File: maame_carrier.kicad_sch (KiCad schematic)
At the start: 43 parts, among them J1 To Kakute H7 V1.5: left strip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, J10 FS-iA10B iBUS servo lead (S +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, J11 TF-Luna pin order 1-6 (CFG ti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, J12 Spare FC I2C (5 V supply, sha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, J13 Payload servo power (+ -); se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, J17 Kakute spare: T3 RSSI 3V3(FC)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, J18 Pi SPI0, 3V3 logic, J3 VBAT tap from ESC battery pad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, J6 Spare power: 5V_AUX G 5V_FC G, J7 Pi expansion: 3V3 logic ONLY, J8 TBS M10Q: order matches its p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, J9 SiK radio (UART4), U1 Raspberry Pi Zero W v1.1, com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, U2 TPS54360BDDAR 60V 3.5A buck

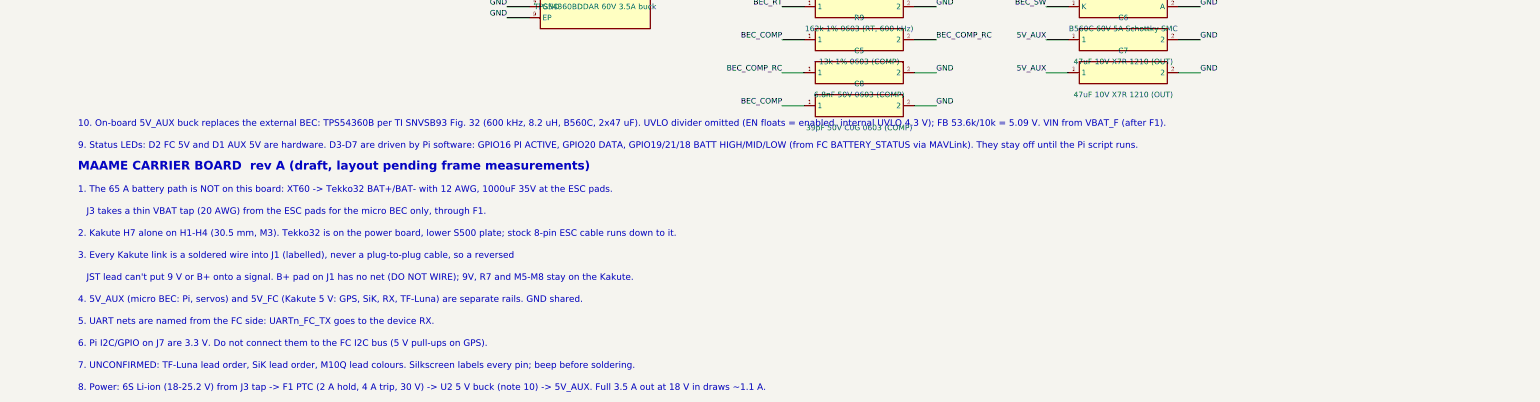
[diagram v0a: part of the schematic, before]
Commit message: D9 SMBJ30A TVS (C113998) on fused VBAT at the buck input; re-routed, DRC 0 errors; fab files regenerated
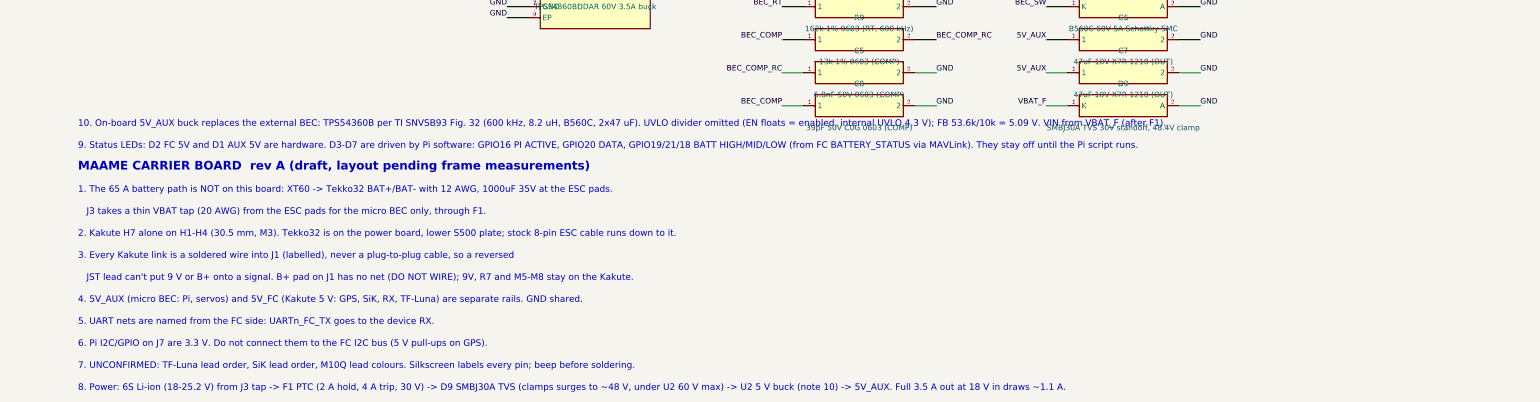
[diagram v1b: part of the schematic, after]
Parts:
- added D9: SMBJ30A TVS 30V standoff, 48.4V clamp, Diode_SMD:D_SMB, symbol maame_carrier:TVS
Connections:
- net GND: now also D9.2 (A)
- net VBAT_F: now also D9.1 (K)
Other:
- note added: "8. Power: 6S Li-ion (18-25.2 V) from J3 tap -> F1 PTC (2 A hold, 4 A trip, 30 V) -> D9 SMBJ30A TVS (clamps surges to ~48 V, under U2 60 V max) -> U2 5 V buck (note 10) -> 5V_AUX. Full 3.5 A out at 18 V in draws ~1.1 A."
- note removed: "8. Power: 6S Li-ion (18-25.2 V) from J3 tap -> F1 PTC (2 A hold, 4 A trip, 30 V) -> U2 5 V buck (note 10) -> 5V_AUX. Full 3.5 A out at 18 V in draws ~1.1 A."
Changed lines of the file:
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@@
 		)
 	)
-	(text "8. Power: 6S Li-ion (18-25.2 V) from J3 tap -> F1 PTC (2 A hold, 4 A trip, 30 V) -> U2 5 V buck (note 10) -> 5V_AUX. Full 3.5 A out at 18 V in draws ~1.1 A."
+	(text "8. Power: 6S Li-ion (18-25.2 V) from J3 tap -> F1 PTC (2 A hold, 4 A trip, 30 V) -> D9 SMBJ30A TVS (clamps surges to ~48 V, under U2 60 V max) -> U2 5 V buck (note 10) -> 5V_AUX. Full 3.5 A out at 18 V in draws ~1.1 A."
 		(exclude_from_sim no)
 		(at 20.32 294.64 0)
@@
 		)
 	)
+	(symbol
+		(lib_id "maame_carrier:TVS")
+		(at 261.62 228.6 0)
+		(unit 1)
+		(body_style 1)
+		(exclude_from_sim no)
+		(in_bom yes)
+		(on_board yes)
+		(in_pos_files yes)
+		(dnp no)
+		(property "Reference" "D9"
+			(at 261.62 223.52 0)
+			(show_name no)
+			(do_not_autoplace no)
+			(effects
+				(font
+					(size 1.27 1.27)
+				)
+			)
+		)
+		(property "Value" "SMBJ30A TVS 30V standoff, 48.4V clamp"
+			(at 261.62 233.68 0)
+			(show_name no)
+			(do_not_autoplace no)
+			(effects
+				(font
+					(size 1.27 1.27)
+				)
+			)
+		)
+		(property "Footprint" "Diode_SMD:D_SMB"
+			(at 261.62 228.6 0)
+			(hide yes)
+			(show_name no)
+			(do_not_autoplace no)
+			(effects
+				(font
+					(size 1.27 1.27)
+				)
+			)
+		)
+		(property "Datasheet" ""
+			(at 261.62 228.6 0)
+			(hide yes)
+			(show_name no)
+			(do_not_autoplace no)
+			(effects
+				(font
+					(size 1.27 1.27)
+				)
+			)
+		)
+		(property "Description" ""
+			(at 261.62 228.6 0)
+			(hide yes)
+			(show_name no)
+			(do_not_autoplace no)
+			(effects
+				(font
+					(size 1.27 1.27)
+				)
+			)
+		)
+		(property "LCSC" "C113998"
+			(at 261.62 228.6 0)
+			(hide yes)
+			(show_name no)
+			(do_not_autoplace no)
+			(effects
+				(font
+					(size 1.27 1.27)
+				)
+			)
+		)
+		(pin "1"
+		)
+		(pin "2"
+		)
+		(instances
+			(project "maame_carrier"
+				(path "/347efe6d-e5df-5320-8613-16be4824f8d1"
+					(reference "D9")
+					(unit 1)
+				)
+			)
+		)
+	)
 	(wire
 		(pts
@@
 			)
 			(justify left bottom)
+		)
+	)
+	(wire
+		(pts
+			(xy 248.92 228.6) (xy 243.84 228.6)
+		)
+		(stroke
+			(width 0)
+			(type default)
+		)
+	)
+	(label "VBAT_F"
+		(at 243.84 228.6 180)
+		(effects
+			(font
+				(size 1.27 1.27)
+			)
+			(justify right bottom)
+		)
+	)
+	(wire
+		(pts
+			(xy 274.32 228.6) (xy 279.4 228.6)
+		)
+		(stroke
+			(width 0)
+			(type default)
+		)
+	)
+	(label "GND"
+		(at 279.4 228.6 0)
+		(effects
+			(font
+				(size 1.27 1.27)
+			)
+			(justify left bottom)

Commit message: Battery labels (6S Li-ion/LiPo 18-25.2 V); J20 VBAT OUT JST-XH via its own F2 2 A PTC; re-routed, DRC 0 errors; fab files regenerated
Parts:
- added F2: PTC fuse 1812 30V 2A hold 4A trip (BSMD1812-200-3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, Fuse:Fuse_1812_4532Metric_Pad1.30x3.40mm_HandSolder, symbol maame_carrier:Fuse
- added J20: VBAT OUT 6S fused (JST-XH 2-pin), Connector_JST:JST_XH_B2B-XH-A_1x02_P2.50mm_Vertical, symbol maame_carrier:BEC_OUT
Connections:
- net GND: now also J20.2 (OUT-)
- net VBAT: now also F2.1
- new net VBAT_OUT_F: F2.2, J20.1 (OUT+)
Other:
- note added: "8. Power: 6S Li-ion (18-25.2 V) from J3 tap -> F1 PTC (2 A hold, 4 A trip, 30 V) -> D9 SMBJ30A TVS (clamps surges to ~48 V, under U2 60 V max) -> U2 5 V buck (note 10) -> 5V_AUX. J20 VBAT OUT (JST-XH) takes VBAT before F1 through its own F2 (2 A). Battery: 6S Li-ion/LiPo only, 18-25.2 V (22.2 V nom). Full 3.5 A out at 18 V in draws ~1.1 A."
- note removed: "8. Power: 6S Li-ion (18-25.2 V) from J3 tap -> F1 PTC (2 A hold, 4 A trip, 30 V) -> D9 SMBJ30A TVS (clamps surges to ~48 V, under U2 60 V max) -> U2 5 V buck (note 10) -> 5V_AUX. Full 3.5 A out at 18 V in draws ~1.1 A."
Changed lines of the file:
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@@
 		)
 	)
-	(text "8. Power: 6S Li-ion (18-25.2 V) from J3 tap -> F1 PTC (2 A hold, 4 A trip, 30 V) -> D9 SMBJ30A TVS (clamps surges to ~48 V, under U2 60 V max) -> U2 5 V buck (note 10) -> 5V_AUX. Full 3.5 A out at 18 V in draws ~1.1 A."
+	(text "8. Power: 6S Li-ion (18-25.2 V) from J3 tap -> F1 PTC (2 A hold, 4 A trip, 30 V) -> D9 SMBJ30A TVS (clamps surges to ~48 V, under U2 60 V max) -> U2 5 V buck (note 10) -> 5V_AUX. J20 VBAT OUT (JST-XH) takes VBAT before F1 through its own F2 (2 A). Battery: 6S Li-ion/LiPo only, 18-25.2 V (22.2 V nom). Full 3.5 A out at 18 V in draws ~1.1 A."
 		(exclude_from_sim no)
 		(at 20.32 294.64 0)
@@
 	)
 	(symbol
+		(lib_id "maame_carrier:Fuse")
+		(at 101.6 144.78 0)
+		(unit 1)
+		(body_style 1)
+		(exclude_from_sim no)
+		(in_bom yes)
+		(on_board yes)
+		(in_pos_files yes)
+		(dnp no)
+		(property "Reference" "F2"
+			(at 101.6 139.7 0)
+			(show_name no)
+			(do_not_autoplace no)
+			(effects
+				(font
+					(size 1.27 1.27)
+					(bold yes)
+				)
+			)
+		)
+		(property "Value" "PTC fuse 1812 30V 2A hold 4A trip (BSMD1812-200-30V) - VBAT OUT"
+			(at 101.6 149.86 0)
+			(show_name no)
+			(do_not_autoplace no)
+			(effects
+				(font
+					(size 1.27 1.27)
+				)
+			)
+		)
+		(property "Footprint" "Fuse:Fuse_1812_4532Metric_Pad1.30x3.40mm_HandSolder"
+			(at 101.6 144.78 0)
+			(hide yes)
+			(show_name no)
+			(do_not_autoplace no)
+			(effects
+				(font
+					(size 1.27 1.27)
+				)
+			)
+		)
+		(property "Datasheet" ""
+			(at 101.6 144.78 0)
+			(hide yes)
+			(show_name no)
+			(do_not_autoplace no)
+			(effects
+				(font
+					(size 1.27 1.27)
+				)
+			)
+		)
+		(property "Description" ""
+			(at 101.6 144.78 0)
+			(show_name no)
+			(do_not_autoplace no)
+			(effects
+				(font
+					(size 1.27 1.27)
+				)
+			)
+		)
+		(property "LCSC" "C960026"
+			(at 101.6 144.78 0)
+			(hide yes)
+			(show_name no)
+			(do_not_autoplace no)
+			(effects
+				(font
+					(size 1.27 1.27)
+				)
+			)
+		)
+		(pin "1"
+		)
+		(pin "2"
+		)
+		(instances
+			(project "maame_carrier"
+				(path "/347efe6d-e5df-5320-8613-16be4824f8d1"
+					(reference "F2")
+					(unit 1)
+				)
+			)
+		)
+	)
+	(symbol
 		(lib_id "maame_carrier:TF_LUNA")
 		(at 177.8 106.68 0)
@@
 		)
 	)
+	(symbol
+		(lib_id "maame_carrier:BEC_OUT")
+		(at 152.4 132.08 0)
+		(unit 1)
+		(body_style 1)
+		(exclude_from_sim no)
+		(in_bom no)
+		(on_board yes)
+		(in_pos_files yes)
+		(dnp yes)
+		(property "Reference" "J20"
+			(at 152.4 127 0)
+			(show_name no)
+			(do_not_autoplace no)
+			(effects
+				(font
+					(size 1.27 1.27)
+					(bold yes)
+				)
+			)
+		)
+		(property "Value" "VBAT OUT 6S fused (JST-XH 2-pin)"
+			(at 152.4 139.7 0)
+			(show_name no)
+			(do_not_autoplace no)
+			(effects
+				(font
+					(size 1.27 1.27)
+				)
+			)
+		)
+		(property "Footprint" "Connector_JST:JST_XH_B2B-XH-A_1x02_P2.50mm_Vertical"
+			(at 152.4 132.08 0)
+			(hide yes)
+			(show_name no)
+			(do_not_autoplace no)
+			(effects
+				(font
+					(size 1.27 1.27)
+				)
+			)
+		)
+		(property "Datasheet" ""
+			(at 152.4 132.08 0)
+			(hide yes)
+			(show_name no)
+			(do_not_autoplace no)
+			(effects
+				(font
+					(size 1.27 1.27)
+				)
+			)
+		)
+		(property "Description" ""
+			(at 152.4 132.08 0)
+			(show_name no)
+			(do_not_autoplace no)
+			(effects
+				(font
+					(size 1.27 1.27)
+				)
+			)
+		)
+		(pin "1"
+		)
+		(pin "2"
+		)
+		(instances
+			(project "maame_carrier"
+				(path "/347efe6d-e5df-5320-8613-16be4824f8d1"
+					(reference "J20")
+					(unit 1)
+				)
+			)
+		)
+	)
 	(no_connect
 		(at 63.5 66.04)
@@
 		)
 	)
+	(wire
+		(pts
+			(xy 88.9 144.78) (xy 83.82 144.78)
+		)
+		(stroke
+			(width 0)
+			(type default)
+		)
+	)
+	(label "VBAT"
+		(at 83.82 144.78 180)
+		(effects
+			(font
+				(size 1.27 1.27)
+			)
+			(justify right bottom)
+		)
+	)
+	(wire
+		(pts
+			(xy 114.3 144.78) (xy 119.38 144.78)
+		)
+		(stroke
+			(width 0)
+			(type default)
+		)
+	)
+	(label "VBAT_OUT_F"
+		(at 119.38 144.78 0)
+		(effects
+			(font
+				(size 1.27 1.27)
+			)
+			(justify left bottom)
+		)
+	)
+	(wire
+		(pts
+			(xy 139.7 132.08) (xy 134.62 132.08)
+		)
+		(stroke
+			(width 0)
+			(type default)
+		)
+	)
+	(label "VBAT_OUT_F"
+		(at 134.62 132.08 180)
+		(effects
+			(font
+				(size 1.27 1.27)
+			)
+			(justify right bottom)
+		)
+	)
+	(wire
+		(pts
+			(xy 139.7 134.62) (xy 134.62 134.62)
+		)
+		(stroke
+			(width 0)
+			(type default)
+		)
+	)
+	(label "GND"
+		(at 134.62 134.62 180)
+		(effects
+			(font
+				(size 1.27 1.27)
+			)
+			(justify right bottom)
+		)
+	)

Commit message: 12 V 2 A on-board buck (U3, TPS54360B) + 12V LED, J21 9V OUT (Kakute VTX 9V via J1 pad 30), J22 12V OUT; F1 -> 3 A/30 V 2920; Pi courtyard limited to socket+standoffs; DSN class patch fixed; re-routed, DRC 0 errors; fab regenerated
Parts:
- added C10, C9: 2.2uF 100V X7R 1210 (12V VIN), Capacitor_SMD:C_1210_3225Metric, symbol maame_carrier:Capacitor
- added C11: 100nF 50V 0603 (12V BOOT), Capacitor_SMD:C_0603_1608Metric, symbol maame_carrier:Capacitor
- added C12: 15nF 50V 0603 (12V COMP), Capacitor_SMD:C_0603_1608Metric, symbol maame_carrier:Capacitor
- added C13: 56pF 50V C0G 0603 (12V COMP), Capacitor_SMD:C_0603_1608Metric, symbol maame_carrier:Capacitor
- added C14, C15: 22uF 25V X7R 1210 (12V OUT), Capacitor_SMD:C_1210_3225Metric, symbol maame_carrier:Capacitor
- added D10: B560C 60V 5A Schottky SMC, Diode_SMD:D_SMC, symbol maame_carrier:Schottky
- added D11: Green 0805: 12V_AUX on, LED_SMD:LED_0805_2012Metric_Pad1.15x1.40mm_HandSolder, symbol maame_carrier:LED
- added J21: 9V OUT from Kakute VTX 9V (JST-XH), Connector_JST:JST_XH_B2B-XH-A_1x02_P2.50mm_Vertical, symbol maame_carrier:BEC_OUT
- added J22: 12V OUT 2A (JST-XH), Connector_JST:JST_XH_B2B-XH-A_1x02_P2.50mm_Vertical, symbol maame_carrier:BEC_OUT
- added L2: 22uH 5.9A Coilcraft XAL6060-223MEC, Inductor_SMD:L_Coilcraft_XAL6060-XXX, symbol maame_carrier:Inductor
- added R12: 162k 1% 0603 (12V RT, 600 kHz), Resistor_SMD:R_0603_1608Metric, symbol maame_carrier:Resistor
- added R13: 9.1k 1% 0603 (12V COMP), Resistor_SMD:R_0603_1608Metric, symbol maame_carrier:Resistor
- added R14: 140k 1% 0603 (12V FB top), Resistor_SMD:R_0603_1608Metric, symbol maame_carrier:Resistor
- added R15: 10k 1% 0603 (12V FB bottom), Resistor_SMD:R_0603_1608Metric, symbol maame_carrier:Resistor
- added R16: 2.2k 0805 (12V LED), Resistor_SMD:R_0805_2012Metric_Pad1.20x1.40mm_HandSolder, symbol maame_carrier:Resistor
- added U3: TPS54360BDDAR 12V 2A buck, Package_SO:TI_SO-PowerPAD-8_ThermalVias, symbol maame_carrier:TPS54360B
- F1: value PTC fuse 1812 30V 2A hold 4A trip (BSMD1812-200-30V, LCSC C960026) -> PTC fuse 2920 30V 3A hold 6A trip (BSMD2920-300-30V, LCSC C7190311); footprint Fuse:Fuse_1812_4532Metric_Pad1.30x3.40mm_HandSolder -> Fuse:Fuse_2920_7451Metric; LCSC C960026 -> C7190311
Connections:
- net GND: now also C10.2, C12.2, C13.2, C14.2, C15.2, C9.2, D10.2 (A), D11.1 (K), J21.2 (OUT-), J22.2 (OUT-), R12.2, R15.2, U3.7 (GND), U3.9 (EP)
- net VBAT_F: now also C10.1, C9.1, U3.2 (VIN)
- new net 12V_AUX: C14.1, C15.1, J22.1 (OUT+), L2.2, R14.1, R16.1
- new net 9V_FC: J1.30 (9V), J21.1 (OUT+)
- new net BEC12_BOOT: C11.1, U3.1 (BOOT)
- new net BEC12_COMP: C13.1, R13.1, U3.6 (COMP)
- new net BEC12_COMP_RC: C12.1, R13.2
- new net BEC12_FB: R14.2, R15.1, U3.5 (FB)
- new net BEC12_RT: R12.1, U3.4 (RT/CLK)
- new net BEC12_SW: C11.2, D10.1 (K), L2.1, U3.8 (SW)
- new net LED11_A: D11.2 (A), R16.2
- no-connect marks 8 -> 9
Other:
- note added: "11. 12V_AUX: second TPS54360B, 12 V 2 A from VBAT_F. Values from TI SNVSB93 eqs 28-51: 600 kHz (162k), L 22 uH (Isat 5.9 A), Cout 2x22 uF 25 V, FB 140k/10k = 12.0 V, comp 9.1k + 15 nF, 56 pF. 9V_FC = Kakute VTX 9 V (J1 pad 30), current per Holybro spec (unconfirmed). F1 3 A hold: 5 V full (1.1 A) + 12 V full (1.5 A) at 18 V in = 2.6 A."
- note added: "8. Power: 6S Li-ion (18-25.2 V) from J3 tap -> F1 PTC (3 A hold, 6 A trip, 30 V, 2920) -> D9 SMBJ30A TVS (clamps surges to ~48 V, under U2 60 V max) -> U2 5 V buck (note 10) -> 5V_AUX. J20 VBAT OUT (JST-XH) takes VBAT before F1 through its own F2 (2 A). Battery: 6S Li-ion/LiPo only, 18-25.2 V (22.2 V nom). Full 3.5 A out at 18 V in draws ~1.1 A."
- note removed: "8. Power: 6S Li-ion (18-25.2 V) from J3 tap -> F1 PTC (2 A hold, 4 A trip, 30 V) -> D9 SMBJ30A TVS (clamps surges to ~48 V, under U2 60 V max) -> U2 5 V buck (note 10) -> 5V_AUX. J20 VBAT OUT (JST-XH) takes VBAT before F1 through its own F2 (2 A). Battery: 6S Li-ion/LiPo only, 18-25.2 V (22.2 V nom). Full 3.5 A out at 18 V in draws ~1.1 A."
